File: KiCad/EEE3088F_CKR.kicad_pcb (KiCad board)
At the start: 2 copper layers, 100 x 100 mm, 127 parts, among them J1 Conn_01x02_Pin, J2 Conn_01x02_Pin, J4 Debugger, Q1 AO3401A, Q2 AO3401A, Q3 AO3401A, Q4 AO3401A, Q5 AO3401A, Q6 AO3401A, Q7 AO3401A, SW1 Reset switch, SW2 switch, SW3 switch, SW4 switch, U1 Battery Charger, U2 LMV321, U3 XC6206PxxxMR, U4 GXHTC3, U5 LTR-303ALS-01, U7 24LC256, U8 usb, U9 HT42B534-2, u6 battery holder

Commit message: a few random vias
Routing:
- net GND: vias 6 -> 12
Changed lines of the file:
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@@
     (fp_arc (start 1.080188 -0.709627) (mid 1.299286 -0.618875) (end 1.390018 -0.399772)
       (stroke (width 0.254) (type solid)) (layer "F.SilkS"))
-    (fp_arc (start 1.390018 0.400203) (mid 1.299267 0.61928) (end 1.080188 0.710033)
+    (fp_arc (start 1.390018 0.400203) (mid 1.299267 0.619284) (end 1.080188 0.710033)
       (stroke (width 0.254) (type solid)) (layer "F.SilkS"))
     (fp_circle (center -0.800102 0.400051) (end -0.77013 0.400051)
@@
     (fp_arc (start 1.080188 -0.709627) (mid 1.299286 -0.618875) (end 1.390018 -0.399772)
       (stroke (width 0.254) (type solid)) (layer "F.SilkS"))
-    (fp_arc (start 1.390018 0.400203) (mid 1.299267 0.61928) (end 1.080188 0.710033)
+    (fp_arc (start 1.390018 0.400203) (mid 1.299267 0.619284) (end 1.080188 0.710033)
       (stroke (width 0.254) (type solid)) (layer "F.SilkS"))
     (fp_circle (center -0.800102 0.400051) (end -0.77013 0.400051)
@@
     (fp_arc (start 1.080188 -0.709627) (mid 1.299286 -0.618875) (end 1.390018 -0.399772)
       (stroke (width 0.254) (type solid)) (layer "F.SilkS"))
-    (fp_arc (start 1.390018 0.400203) (mid 1.299267 0.61928) (end 1.080188 0.710033)
+    (fp_arc (start 1.390018 0.400203) (mid 1.299267 0.619284) (end 1.080188 0.710033)
       (stroke (width 0.254) (type solid)) (layer "F.SilkS"))
     (fp_circle (center -0.800102 0.400051) (end -0.77013 0.400051)
@@
     (fp_arc (start 1.080188 -0.709627) (mid 1.299286 -0.618875) (end 1.390018 -0.399772)
       (stroke (width 0.254) (type solid)) (layer "F.SilkS"))
-    (fp_arc (start 1.390018 0.400203) (mid 1.299267 0.619284) (end 1.080188 0.710033)
+    (fp_arc (start 1.390018 0.400203) (mid 1.299267 0.61928) (end 1.080188 0.710033)
       (stroke (width 0.254) (type solid)) (layer "F.SilkS"))
     (fp_circle (center -0.800102 0.400051) (end -0.77013 0.400051)
@@
   )
   (via (at -110.5 116) (size 0.8) (drill 0.4) (layers "F.Cu" "B.Cu") (free) (net 1))
+  (via (at -100.5 95.5) (size 0.8) (drill 0.4) (layers "F.Cu" "B.Cu") (free) (net 1))
+  (via (at -117.5 88.5) (size 0.8) (drill 0.4) (layers "F.Cu" "B.Cu") (free) (net 1))
   (via (at -111 123) (size 0.8) (drill 0.4) (layers "F.Cu" "B.Cu") (free) (net 1))
+  (via (at -118 79.5) (size 0.8) (drill 0.4) (layers "F.Cu" "B.Cu") (free) (net 1))
+  (via (at -105.5 125) (size 0.8) (drill 0.4) (layers "F.Cu" "B.Cu") (free) (net 1))
+  (via (at -97.5 110.5) (size 0.8) (drill 0.4) (layers "F.Cu" "B.Cu") (free) (net 1))
+  (via (at -71.5 113) (size 0.8) (drill 0.4) (layers "F.Cu" "B.Cu") (free) (net 1))
   (via (at -111.5 93) (size 0.8) (drill 0.4) (layers "F.Cu" "B.Cu") (free) (net 1))
   (via (at -110 120.5) (size 0.8) (drill 0.4) (layers "F.Cu" "B.Cu") (free) (net 1))

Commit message: week 5 writeup and a lot of changes to PCB design
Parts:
- moved U2 212.3 mm to (166.2, 83.0)
- moved R10 212.3 mm to (179.5, 74.0)
- moved C4 211.3 mm to (172.8, 99.4)
- moved D2 211.3 mm to (159.4, 82.9)
- moved R13 211.3 mm to (180.1, 65.7)
- moved R16 211.3 mm to (165.8, 62.8)
- moved R19 211.3 mm to (168.1, 66.4)
- moved R48 211.3 mm to (145.2, 78.1)
- moved R49 211.3 mm to (145.1, 75.6)
- moved R55 211.3 mm to (124.7, 123.9)
- moved R56 211.3 mm to (146.3, 93.3)
- moved R57 211.3 mm to (146.3, 90.8)
- moved R6 211.3 mm to (159.4, 78.5)
- moved R63 211.3 mm to (145.1, 95.9)
- moved R64 211.3 mm to (124.0, 118.8)
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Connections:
- U1 pad 9: (no net) -> GND
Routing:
- net /Microcontroller/SDA_2: track 48.8 -> 65.7 mm
- net GND: track 5.60 -> 19.7 mm, vias 12 -> 45
- net /Microcontroller/SCL_1: track 96.3 -> 108.5 mm, vias 3 -> 5
- net Net-(U1-BAT): track 31.9 -> 37.8 mm
- net +3V3: track 391.3 -> 387.8 mm
- net /Sensors/Light_SCL: track 13.8 -> 16.8 mm
- net Net-(U7-SCL): track 12.3 -> 14.9 mm
- net Net-(#FLG06-pwr): track 13.1 -> 15.5 mm
- net Net-(U2-+): track 5.48 -> 7.36 mm
- net /Microcontroller/SDA_1: track 83.9 -> 85.6 mm, vias 3 -> 5
- net Net-(U2--): track 7.32 -> 8.80 mm, vias 0 -> 2
- net Net-(U1-PROG): track 1.69 -> 3.16 mm
- net /Microcontroller/INT_1: track 64.1 -> 65.4 mm, vias 1 -> 3
- net /Microcontroller/Lght_P_1: track 26.1 -> 24.8 mm
- net Net-(U7-SDA): track 9.53 -> 10.6 mm
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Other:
- board text added: "Robert Dugmore DGMROB001 Cameron Clark CLRCAM007 Kian Frassek FRSKIA001 EEE3088F Sensor PCB v0.1"

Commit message: powwer 5v line seperation
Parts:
- moved U2 212.3 mm to (-45.7, 96.5)
- moved R10 212.3 mm to (-32.3, 88.5)
- moved C4 211.3 mm to (-38.1, 112.9)
- moved D2 211.3 mm to (-51.5, 96.4)
- moved R13 211.3 mm to (-30.8, 79.2)
- moved R16 211.3 mm to (-45.0, 76.3)
- moved R19 211.3 mm to (-42.8, 79.9)
- moved R48 211.3 mm to (-65.7, 91.6)
- moved R49 211.3 mm to (-65.8, 89.1)
- moved R55 211.3 mm to (-86.2, 137.4)
- moved R56 211.3 mm to (-64.6, 106.8)
- moved R57 211.3 mm to (-64.6, 104.3)
- moved R6 211.3 mm to (-51.5, 92.0)
- moved R63 211.3 mm to (-65.8, 109.4)
- moved R64 211.3 mm to (-86.9, 132.3)
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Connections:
- U1 pad 9: GND -> (no net)
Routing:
- net /Microcontroller/SDA_2: track 65.7 -> 48.8 mm
- net GND: track 19.7 -> 5.60 mm, vias 45 -> 12
- net /Microcontroller/SCL_1: track 108.5 -> 96.3 mm, vias 5 -> 3
- net Net-(U1-BAT): track 37.8 -> 31.9 mm
- net +3V3: track 387.8 -> 391.3 mm
- net /Sensors/Light_SCL: track 16.8 -> 13.8 mm
- net Net-(U7-SCL): track 14.9 -> 12.3 mm
- net Net-(#FLG06-pwr): track 15.5 -> 13.1 mm
- net Net-(U2-+): track 7.36 -> 5.48 mm
- net /Microcontroller/SDA_1: track 85.6 -> 83.9 mm, vias 5 -> 3
- net Net-(U2--): track 8.80 -> 7.32 mm, vias 2 -> 0
- net Net-(U1-PROG): track 3.16 -> 1.69 mm
- net /Microcontroller/INT_1: track 65.4 -> 64.1 mm, vias 3 -> 1
- net /Microcontroller/Lght_P_1: track 24.8 -> 26.1 mm
- net Net-(U7-SDA): track 10.6 -> 9.53 mm
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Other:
- board text removed: "Robert Dugmore DGMROB001 Cameron Clark CLRCAM007 Kian Frassek FRSKIA001 EEE3088F Sensor PCB v0.1"

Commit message: Final schematic changes and start board design
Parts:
- removed R63: 8.2k, footprint:R0402
- removed R64: 10k, footprint:R0805
- removed R65, R66, R67, R68, R69, R70, R71, R72: 0, footprint:R0603
- removed TP23: STM32 Tx, footprint:Testpoint_2.54mm
- removed TP24: STM32 Rx, footprint:Testpoint_2.54mm
- removed TP25: EEPROM SDA, footprint:Testpoint_2.54mm
- removed TP26: EEPROM SCL, footprint:Testpoint_2.54mm
- removed TP27: USB D-, footprint:Testpoint_2.54mm
- removed TP28: USB D+, footprint:Testpoint_2.54mm
- removed U3: XC6206PxxxMR, footprint:SOT-23-3_L2.9-W1.6-P1.90-LS2.8-BR
- removed u6: battery holder, footprint:BATTERY-SMD_18650-1S-L77.1-W20.7-1
- added J5: STM-link_debugger, Connector_PinHeader_2.54mm:PinHeader_1x03_P2.54mm_Vertical, F.Cu at (152.0, 93.1)
- added J6: 01x10_male_header, Connector_PinHeader_2.54mm:PinHeader_1x10_P2.54mm_Vertical, F.Cu at (101.6, 108.2)
- added JP1: 01x02_male_header_jumper, Connector_PinHeader_2.54mm:PinHeader_1x02_P2.54mm_Vertical, F.Cu at (141.4, 85.9)
- added JP2: 01x02_male_header_jumper, Connector_PinHeader_2.54mm:PinHeader_1x02_P2.54mm_Vertical, F.Cu at (146.0, 85.9)
- added JP3: 01x02_male_header_jumper, Connector_PinHeader_2.54mm:PinHeader_1x02_P2.54mm_Vertical, F.Cu at (150.7, 85.9)
- added JP4: 01x02_male_header_jumper, Connector_PinHeader_2.54mm:PinHeader_1x02_P2.54mm_Vertical, F.Cu at (155.3, 85.9)
- added JP5: 01x03_male_header_jumper, Connector_PinHeader_2.54mm:PinHeader_1x03_P2.54mm_Vertical, F.Cu at (106.2, 108.2)
- added JP6: 01x03_male_header_jumper, Connector_PinHeader_2.54mm:PinHeader_1x03_P2.54mm_Vertical, F.Cu at (110.9, 108.2)
- added Q8: AO3401A, JLCPartFootprints:SOT-23_L2.9-W1.3-P1.90-LS2.4-BR, F.Cu at (128.9, 120.8)
- added R51: 3.9k, JLCPartFootprints:R0402, F.Cu at (149.9, 62.3)
- added R54: 8.2k, JLCPartFootprints:R0402, F.Cu at (149.9, 64.4)
- added R59: 0, JLCPartFootprints:R0603, F.Cu at (148.9, 77.4)
- added R60: 10k, JLCPartFootprints:R0805, F.Cu at (112.9, 131.5)
- added R61: 20k, JLCPartFootprints:R0603, F.Cu at (115.2, 107.1)
- added R62: 0, JLCPartFootprints:R0603, F.Cu at (115.2, 109.6)
- added TP12: LED 2, CustomFootprints:Testpoint, F.Cu at (150.2, 46.3)
- added TP13: Switch 1, CustomFootprints:Testpoint, F.Cu at (150.2, 50.0)
- added U6: LTR-303ALS-01, JLCPartFootprints:SOT-363_L2.0-W1.3-P0.65-LS2.1-BL, F.Cu at (142.7, 122.3)
- added u3: battery holder, JLCPartFootprints:BATTERY-SMD_18650-1S-L77.1-W20.7-1, F.Cu at (74.5, 85.2)
- C1, C2, C3, C4: value 10uf -> 10u; footprint footprint:C0603 -> JLCPartFootprints:C0603
- C5: footprint footprint:C0402_NEW -> JLCPartFootprints:C0402
- C6: footprint footprint:C0402 -> JLCPartFootprints:C0402
- D1: value LED Green -> zener diode; footprint footprint:LED0805-R-RD -> JLCPartFootprints:SOD-123_L2.8-W1.8-LS3.7-RD
- D2: value zener diode -> LED_green; footprint footprint:SOD-123_L2.8-W1.8-LS3.7-RD -> JLCPartFootprints:LED0603-RD
- D3: value LED RED -> LED_red; footprint footprint:LED0603-RD -> JLCPartFootprints:LED0603-RD
- D4, D5: value LED -> LED_white; footprint footprint:LED0603-RD -> JLCPartFootprints:LED0805-R-RD
- J1, J2: value Conn_01x02_Pin -> 01x02_male_header; footprint footprint:HDR-TH_2P-P2.54-V-M -> Connector_PinHeader_2.54mm:PinHeader_1x02_P2.54mm_Vertical
- J3: value ~ -> STM32F051C6_female_header; footprint footprint:STM32F051C6_female_header -> CustomFootprints:STM32F051C6_female_header
- J4: value Debugger -> STM32F051C6_testpoints; footprint footprint:HDR-TH_3P-P2.54_CS-1165SDIG -> CustomFootprints:STM32F051C6_testpoints
- Q1, Q2, Q3, Q4, Q5, Q6, Q7: footprint footprint:SOT-23_L2.9-W1.3-P1.90-LS2.4-BR -> JLCPartFootprints:SOT-23_L2.9-W1.3-P1.90-LS2.4-BR
- R1, R16, R18, R2, R20, R21, R23, R24, R26, R27, R29, R30, R31, R32, R33, R34, R35, R36, R37, R40, R41, R42, R43, R44, R45, R46, R47: footprint footprint:R0603 -> JLCPartFootprints:R0603
- R10, R15, R19, R56, R57: value 1.2k -> 0; footprint footprint:R0805 -> JLCPartFootprints:R0603
- R11, R3: value R1M -> 1.2k; footprint footprint:R0805 -> JLCPartFootprints:R0805
- R12: value R3M -> 1M; footprint footprint:R0603 -> JLCPartFootprints:R0805
- R13: value 0 -> 3M; footprint footprint:R0603 -> JLCPartFootprints:R0603
- R14, R17, R22, R38, R39, R9: value 0 -> 1.2k; footprint footprint:R0603 -> JLCPartFootprints:R0805
- R25: value 100k -> 0; footprint footprint:R1206 -> JLCPartFootprints:R0603
- R28: value 0 -> 100k; footprint footprint:R0603 -> JLCPartFootprints:R1206
- R4: value R2M -> 0; footprint footprint:R0805 -> JLCPartFootprints:R0603
- R48, R55: value 3.9k -> 0; footprint footprint:R0402 -> JLCPartFootprints:R0603
- R49: value 3.9k -> 10k; footprint footprint:R0402 -> JLCPartFootprints:R0805
- R5: value 1.2k -> 1M; footprint footprint:R0805 -> JLCPartFootprints:R0805
- R50, TH1: footprint footprint:R0402 -> JLCPartFootprints:R0402
- R58: value 8.2k -> 0; footprint footprint:R0402 -> JLCPartFootprints:R0603
- R6: value 27.5k -> 2M; footprint footprint:R0805 -> JLCPartFootprints:R0805
- R7: value 10k -> 27.5k; footprint footprint:R0805 -> JLCPartFootprints:R0805
- R8: value 1.2k -> 10k; footprint footprint:R0805 -> JLCPartFootprints:R0805
- RV1: footprint footprint:RES-ADJ-TH_RK09K1130AJ3 -> JLCPartFootprints:RES-ADJ-TH_RK09K1130AJ3
- SW1: footprint footprint:SW-SMD_4P-L5.1-W5.1-P3.70-LS6.5-TL-2 -> JLCPartFootprints:SW-SMD_4P-L5.1-W5.1-P3.70-LS6.5-TL-2
- SW2, SW3, SW4: value switch -> Switch; footprint footprint:SW-SMD_4P-L5.1-W5.1-P3.70-LS6.5-TL-2 -> JLCPartFootprints:SW-SMD_4P-L5.1-W5.1-P3.70-LS6.5-TL-2
- TP1, TP5: footprint footprint:Testpoint_2.54mm -> CustomFootprints:Testpoint
- TP10: value Light SCL -> Light Interrupt; footprint footprint:Testpoint_2.54mm -> CustomFootprints:Testpoint
- TP11: value Light Interrupt -> LED 1; footprint footprint:Testpoint_2.54mm -> CustomFootprints:Testpoint
- TP14: value NSRT -> Switch 2; footprint footprint:Testpoint_2.54mm -> CustomFootprints:Testpoint
- TP15: value Switch1 -> Switch 3; footprint footprint:Testpoint_2.54mm -> CustomFootprints:Testpoint
- TP16: value Switch2 -> uc Tx; footprint footprint:Testpoint_2.54mm -> CustomFootprints:Testpoint
- TP17: value Switch3 -> uc Rx; footprint footprint:Testpoint_2.54mm -> CustomFootprints:Testpoint
- TP18: value STM32 3V3 -> Plug Detect; footprint footprint:Testpoint_2.54mm -> CustomFootprints:Testpoint
- TP19: value STM32 LED1 -> EEPROM SDA; footprint footprint:Testpoint_2.54mm -> CustomFootprints:Testpoint
- TP2: value battery charger -> UVLO; footprint footprint:Testpoint_2.54mm -> CustomFootprints:Testpoint
- TP20: value STM32 LED2 -> EEPROM SCL; footprint footprint:Testpoint_2.54mm -> CustomFootprints:Testpoint
- TP21: value STM32 GND -> USB D-; footprint footprint:Testpoint_2.54mm -> CustomFootprints:Testpoint
- TP22: value STM32 BOOT0 -> USB D+; footprint footprint:Testpoint_2.54mm -> CustomFootprints:Testpoint
- TP3: value UVLO -> battery charger; footprint footprint:Testpoint_2.54mm -> CustomFootprints:Testpoint
- TP4: value +battery out -> 3.3v out; footprint footprint:Testpoint_2.54mm -> CustomFootprints:Testpoint
- TP6: value 3.3v out -> Pot ADC; footprint footprint:Testpoint_2.54mm -> CustomFootprints:Testpoint
- TP7: value Pot ADC -> Sensors SDA; footprint footprint:Testpoint_2.54mm -> CustomFootprints:Testpoint
- TP8: value Therm ADC -> Sensors SCL; footprint footprint:Testpoint_2.54mm -> CustomFootprints:Testpoint
- TP9: value Light SDA -> Therm ADC; footprint footprint:Testpoint_2.54mm -> CustomFootprints:Testpoint
- U1: value Battery Charger -> LMV321IDBVR; footprint footprint:ESOP-8_L4.9-W3.9-P1.27-LS6.0-BL-EP -> JLCPartFootprints:SOT-23-5_L3.0-W1.7-P0.95-LS2.8-BR
- U2: value LMV321 -> Battery Charger; footprint footprint:SOT-23-5_L3.0-W1.7-P0.95-LS2.8-BR -> JLCPartFootprints:ESOP-8_L4.9-W3.9-P1.27-LS6.0-BL-EP
- U4: value GXHTC3 -> XC6206PxxxMR; footprint footprint:DFN-6_L2.0-W2.0-P0.50-BL-EP -> JLCPartFootprints:SOT-23-3_L2.9-W1.6-P1.90-LS2.8-BR
- U5: value LTR-303ALS-01 -> GXHTC3; footprint footprint:SOT-363_L2.0-W1.3-P0.65-LS2.1-BL -> JLCPartFootprints:DFN-6_L2.0-W2.0-P0.50-BL-EP
- U7: footprint footprint:PDIP-8_L9.3-W6.4-P2.54-LS7.6-BL -> JLCPartFootprints:PDIP-8_L9.3-W6.4-P2.54-LS7.6-BL
- U8: footprint footprint:MICRO-USB-SMD_MICROXNJ -> JLCPartFootprints:MICRO-USB-SMD_MICROXNJ
- U9: footprint footprint:SOIC-8_L4.9-W3.9-P1.27-LS6.0-BL -> JLCPartFootprints:SOP-8_L4.9-W3.9-P1.27-LS6.0-BL
- moved TP11 269.5 mm to (150.2, 42.7)
- moved R38 265.6 mm to (153.2, 67.8)
- moved C5 256.9 mm to (138.9, 121.5), turned to 0 degrees
- moved U7 256.0 mm to (144.4, 96.0)
- moved R43 255.3 mm to (144.9, 70.0)
- moved R45 255.2 mm to (144.9, 74.9)
- moved C6 255.0 mm to (138.9, 123.7), turned to 0 degrees
- moved R39 254.4 mm to (153.2, 70.7)
- moved R47 253.4 mm to (144.9, 79.9)
- moved R42 252.6 mm to (144.9, 67.5)
- moved TH1 252.5 mm to (142.2, 125.4), turned to 0 degrees
- moved R36 251.7 mm to (141.0, 74.9)
- moved R46 250.8 mm to (144.9, 77.4)
- moved R33 250.6 mm to (141.0, 67.5)
- moved RV1 249.5 mm to (138.3, 115.5)
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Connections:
- C1 pad 1: Net-(D1-A) -> Net-(D2-A)
- C2 pad 1: Net-(U1-BAT) -> Net-(J1-Pin_2)
- C3 pad 1: Net-(#FLG01-pwr) -> Net-(U4-VI)
- C4 pad 1: +3V3 -> Net-(U4-VO)
- C5 pad 1: Net-(#FLG04-pwr) -> Net-(Q7-D)
- C6 pad 1: Net-(#FLG06-pwr) -> Net-(Q8-D)
- D1 pad 1: Net-(D1-K) -> Net-(U1--)
- D1 pad 2: Net-(D1-A) -> Net-(D1-Pad2)
- D2 pad 1: Net-(U2--) -> Net-(D2-K)
- D2 pad 2: Net-(D2-Pad2) -> Net-(D2-A)
- D3 pad 2: Net-(D1-A) -> Net-(D2-A)
- J3 pad 10: /Microcontroller/THM_2 -> /Microcontroller/uc10
- J3 pad 11: /Microcontroller/POT_2 -> /Microcontroller/uc11
- J3 pad 12: /Microcontroller/Tx_2 -> /Microcontroller/uc12
- J3 pad 13: /Microcontroller/Rx_2 -> /Microcontroller/uc13
- J3 pad 14: /Microcontroller/INT_2 -> /Microcontroller/uc14
- J3 pad 15: /Microcontroller/LED1_1 -> /Microcontroller/LED1
- J3 pad 16: /Microcontroller/LED2_1 -> /Microcontroller/LED2
- J3 pad 17: unconnected-(J3-_PA7-Pad17) -> /Microcontroller/uc17
- J3 pad 18: /Microcontroller/THM_1 -> /Microcontroller/THM_uc
- J3 pad 19: /Microcontroller/POT_1 -> /Microcontroller/POT_uc
- J3 pad 2: unconnected-(J3-_PC13-Pad2) -> /Microcontroller/uc2
- J3 pad 20: /Microcontroller/POT_P_1 -> /Microcontroller/POT_P
- J3 pad 21: /Microcontroller/SCL_1 -> /Microcontroller/Plg_Dtct
- J3 pad 22: /Microcontroller/SDA_1 -> /Microcontroller/uc22
- J3 pad 25: /Microcontroller/INT_1 -> /Microcontroller/INT
- J3 pad 29: /Microcontroller/POT_P_2 -> /Microcontroller/uc29
- J3 pad 3: unconnected-(J3-_PC14-Pad3) -> /Microcontroller/uc3
- J3 pad 30: /Microcontroller/THM_P_2 -> /Microcontroller/uc30
- J3 pad 31: /Microcontroller/Lght_P_2 -> /Microcontroller/uc31
- J3 pad 32: /Microcontroller/TeHu_P_2 -> /Microcontroller/uc32
- J3 pad 33: unconnected-(J3-PA12_-Pad33) -> /Microcontroller/uc33
- J3 pad 35: unconnected-(J3-PA6_-Pad35) -> /Microcontroller/uc35
- J3 pad 36: unconnected-(J3-PF7_-Pad36) -> /Microcontroller/uc36
- J3 pad 38: unconnected-(J3-PA15_-Pad38) -> /Microcontroller/uc38
- J3 pad 39: /Microcontroller/THM_P_1 -> /Microcontroller/THM_P
- J3 pad 4: unconnected-(J3-_PC15-Pad4) -> /Microcontroller/uc4
- J3 pad 40: /Microcontroller/Lght_P_1 -> /Microcontroller/Lght_P
- J3 pad 41: /Microcontroller/TeHu_P_1 -> /Microcontroller/TeHu_P
- J3 pad 42: /Microcontroller/Tx_1 -> /Microcontroller/Tx
- J3 pad 43: /Microcontroller/Rx_1 -> /Microcontroller/Rx
- J3 pad 45: /Microcontroller/SCL_2 -> /Microcontroller/SCL_uc
- J3 pad 46: /Microcontroller/SDA_2 -> /Microcontroller/SDA_uc
- J3 pad 5: unconnected-(J3-_PF0-Pad5) -> /Microcontroller/uc5
- J3 pad 6: unconnected-(J3-_PF1-Pad6) -> /Microcontroller/uc6
- J4 pad 1: /Microcontroller/NSRT -> +3V3
- J4 pad 2: /Microcontroller/SWDIO -> /Microcontroller/uc2
- J4 pad 3: /Microcontroller/SWCLK -> /Microcontroller/uc3
- Q1 pad 2: Net-(#FLG02-pwr) -> Net-(D2-A)
- Q1 pad 3: /Power/3.3V UVLO/polarity protector -> Net-(Q1-D)
- Q2 pad 3: Net-(J1-Pin_2) -> /Power/3.3V UVLO/polarity protector
- Q3 pad 2: Net-(Q3-S) -> /Power/polarity protected battery voltage
- Q3 pad 3: /Power/polarity protected battery voltage -> Net-(Q3-D)
- Q4 pad 1: /Microcontroller/Potentiometer_powerenable -> Net-(Q4-G)
- Q4 pad 2: Net-(Q4-S) -> /Power/polarity protected battery voltage
- Q5 pad 1: /Microcontroller/Thermistor_powerenable -> /Microcontroller/Potentiometer_powerenable
- Q6 pad 1: /Microcontroller/TemperatureHumidity_powerenable -> /Microcontroller/Thermistor_powerenable
- Q6 pad 3: Net-(#FLG04-pwr) -> Net-(Q6-D)
- Q7 pad 1: /Microcontroller/Light_powerenable -> /Microcontroller/TemperatureHumidity_powerenable
- Q7 pad 3: Net-(#FLG06-pwr) -> Net-(Q7-D)
- R1 pad 1: Net-(D1-A) -> Net-(Q1-D)
- R10 pad 1: Net-(U1-PROG) -> /Power/polarity protected battery voltage
- R10 pad 2: GND -> /Power/3.3V UVLO/polarity protector
- R11 pad 1: Net-(Q1-G) -> Net-(U2-CHRG)
- R11 pad 2: Net-(R11-Pad2) -> Net-(D3-K)
- R12 pad 1: Net-(R11-Pad2) -> Net-(Q2-G)
- R12 pad 2: Net-(D2-Pad2) -> Net-(R12-Pad2)
- R13 pad 1: Net-(Q2-S) -> Net-(R12-Pad2)
- R13 pad 2: Net-(U1-BAT) -> Net-(D1-Pad2)
- R14 pad 1: Net-(J1-Pin_2) -> Net-(U2-PROG)
- R14 pad 2: Net-(U1-BAT) -> GND
- R15 pad 1: GND -> Net-(Q3-D)
- R15 pad 2: Net-(Q2-G) -> Net-(J1-Pin_2)
- R16 pad 1: Net-(Q3-S) -> /Power/polarity protected battery voltage
- R17 pad 1: Net-(#FLG01-pwr) -> +5V
- R17 pad 2: /Power/3.3V UVLO/polarity protector -> Net-(Q3-G)
- R18 pad 1: /Power/polarity protected battery voltage -> Net-(U4-VI)
- R18 pad 2: Net-(J1-Pin_2) -> /Power/3.3V UVLO/polarity protector
- R19 pad 1: GND -> Net-(U4-VO)
- R19 pad 2: Net-(Q3-G) -> /Power/3.3V UVLO/polarity protector
- R2 pad 1: Net-(#FLG02-pwr) -> Net-(D2-A)
- R2 pad 2: /Power/polarity protected battery voltage -> +5V
- R20 pad 1: +3V3 -> Net-(Q4-D)
- R20 pad 2: Net-(#FLG01-pwr) -> Net-(D2-A)
- R21 pad 1: Net-(Q4-D) -> /Power/polarity protected battery voltage
- R21 pad 2: +3V3 -> Net-(D2-A)
- R22 pad 1: Net-(Q5-D) -> Net-(Q4-G)
- R22 pad 2: +3V3 -> GND
- R23 pad 1: Net-(Q4-S) -> +3V3
- R23 pad 2: +3V3 -> Net-(U4-VO)
- R24 pad 1: Net-(Q5-S) -> Net-(Q5-D)
- R25 pad 1: /Microcontroller/Thermistor_signal -> Net-(Q6-D)
- R25 pad 2: Net-(Q5-D) -> +3V3
- R26 pad 1: Net-(#FLG04-pwr) -> Net-(Q5-S)
- R27 pad 1: Net-(#FLG06-pwr) -> Net-(Q6-S)
- R28 pad 1: Net-(Q6-S) -> /Microcontroller/Thermistor_signal
- R28 pad 2: +3V3 -> Net-(Q6-D)
- R29 pad 1: Net-(Q7-S) -> Net-(Q7-D)
- R3 pad 1: Net-(#FLG02-pwr) -> Net-(Q1-G)
- R3 pad 2: Net-(U2-+) -> GND
- R30 pad 1: /Sensors/Light_SCL -> Net-(Q8-D)
- R30 pad 2: /Microcontroller/SCL_1 -> +3V3
- R31 pad 1: /Sensors/Light_SDA -> Net-(Q7-S)
- R31 pad 2: /Microcontroller/SDA_1 -> +3V3
- R32 pad 1: /Sensors/Light_interrupt -> Net-(Q8-S)
- R32 pad 2: /Microcontroller/INT_1 -> +3V3
- R33 pad 1: /Sensors/Light_SCL -> /Microcontroller/LED1
- R33 pad 2: /Microcontroller/SCL_2 -> Net-(R33-Pad2)
- R34 pad 1: /Sensors/Light_SDA -> /Microcontroller/LED2
- R34 pad 2: /Microcontroller/SDA_2 -> Net-(R34-Pad2)
- R35 pad 1: /Sensors/Light_interrupt -> Net-(R35-Pad1)
- R35 pad 2: /Microcontroller/INT_2 -> /Microcontroller/SW1
- R36 pad 1: /Microcontroller/Thermistor_signal -> Net-(R36-Pad1)
- R36 pad 2: /Microcontroller/THM_1 -> /Microcontroller/SW2
- R37 pad 1: /Microcontroller/Potentiometer_signal -> Net-(R37-Pad1)
- R37 pad 2: /Microcontroller/POT_1 -> /Microcontroller/SW3
- R38 pad 1: /Microcontroller/Thermistor_signal -> Net-(R33-Pad2)
- R38 pad 2: /Microcontroller/THM_2 -> Net-(D4-A)
- R39 pad 1: /Microcontroller/Potentiometer_signal -> Net-(R34-Pad2)
- R39 pad 2: /Microcontroller/POT_2 -> Net-(D5-A)
- R4 pad 1: Net-(U2-+) -> Net-(Q2-S)
- R4 pad 2: GND -> /Power/polarity protected battery voltage
- R40 pad 1: /Microcontroller/Potentiometer_powerenable -> /Sensors/Light_SCL
- R40 pad 2: /Microcontroller/POT_P_1 -> /Microcontroller/SCL
- R41 pad 1: /Microcontroller/Thermistor_powerenable -> /Sensors/Light_SDA
- R41 pad 2: /Microcontroller/THM_P_1 -> /Microcontroller/SDA
- R42 pad 1: /Microcontroller/Light_powerenable -> /Sensors/Light_interrupt
- R42 pad 2: /Microcontroller/Lght_P_1 -> /Microcontroller/INT
- R43 pad 1: /Microcontroller/TemperatureHumidity_powerenable -> /Microcontroller/Thermistor_signal
- R43 pad 2: /Microcontroller/TeHu_P_1 -> /Microcontroller/THM
- R44 pad 1: /Microcontroller/Potentiometer_powerenable -> /Microcontroller/Potentiometer_signal
- R44 pad 2: /Microcontroller/POT_P_2 -> /Microcontroller/POT
- R45 pad 1: /Microcontroller/Thermistor_powerenable -> /Microcontroller/Potentiometer_powerenable
- R45 pad 2: /Microcontroller/THM_P_2 -> /Microcontroller/POT_P
- R46 pad 1: /Microcontroller/Light_powerenable -> /Microcontroller/Thermistor_powerenable
- R46 pad 2: /Microcontroller/Lght_P_2 -> /Microcontroller/THM_P
- R47 pad 1: /Microcontroller/TemperatureHumidity_powerenable -> /Microcontroller/Light_powerenable
- R47 pad 2: /Microcontroller/TeHu_P_2 -> /Microcontroller/Lght_P
- R48 pad 1: /Microcontroller/SCL_1 -> /Microcontroller/TemperatureHumidity_powerenable
- R48 pad 2: +3V3 -> /Microcontroller/TeHu_P
- R49 pad 1: /Microcontroller/SDA_1 -> GND
- R49 pad 2: +3V3 -> /Microcontroller/BOOT0
- R5 pad 1: Net-(D1-K) -> Net-(Q2-S)
- R5 pad 2: Net-(U1-STDBY#) -> Net-(U1-+)
- R50 pad 1: /Microcontroller/SCL_2 -> /Microcontroller/SCL_uc
- R55 pad 1: /Microcontroller/SDA_2 -> /Microcontroller/Tx
- R55 pad 2: +3V3 -> /Microcontroller/Tx
- R56 pad 1: /Microcontroller/LED1_1 -> /Microcontroller/Rx
- R56 pad 2: Net-(D4-A) -> /Microcontroller/Rx
- R57 pad 1: /Microcontroller/LED2_1 -> /Microcontroller/Plug_Detect
- R57 pad 2: Net-(D5-A) -> /Microcontroller/Plg_Dtct
- R58 pad 1: /Microcontroller/INT_1 -> Net-(U7-SDA)
- R58 pad 2: +3V3 -> /Microcontroller/SDA
- R6 pad 1: Net-(#FLG02-pwr) -> Net-(U1-+)
- R6 pad 2: Net-(U2--) -> GND
- R7 pad 1: Net-(D2-Pad2) -> Net-(Q2-S)
- R7 pad 2: GND -> Net-(U1--)
- R8 pad 1: Net-(U1-CHRG) -> Net-(D1-Pad2)
- R8 pad 2: Net-(D3-K) -> GND
- R9 pad 1: /Power/polarity protected battery voltage -> Net-(D2-K)
- R9 pad 2: /Power/3.3V UVLO/polarity protector -> Net-(U2-STDBY#)
- RV1 pad 1: Net-(Q4-D) -> Net-(Q5-D)
- SW2 pad 2: /Microcontroller/SW1 -> Net-(R35-Pad1)
- SW3 pad 2: /Microcontroller/SW2 -> Net-(R36-Pad1)
- SW4 pad 2: /Microcontroller/SW3 -> Net-(R37-Pad1)
- TP1 pad 1: Net-(D1-A) -> Net-(D2-A)
- TP10 pad 1: /Sensors/Light_SCL -> /Sensors/Light_interrupt
- TP11 pad 1: /Sensors/Light_interrupt -> Net-(R33-Pad2)
- TP14 pad 1: /Microcontroller/NSRT -> /Microcontroller/SW2
- TP15 pad 1: /Microcontroller/SW1 -> /Microcontroller/SW3
- TP16 pad 1: /Microcontroller/SW2 -> /Microcontroller/Tx
- TP17 pad 1: /Microcontroller/SW3 -> /Microcontroller/Rx
- TP18 pad 1: +3V3 -> /Microcontroller/Plug_Detect
- TP19 pad 1: /Microcontroller/LED1_1 -> Net-(U7-SCL)
- TP2 pad 1: Net-(U1-BAT) -> /Power/3.3V UVLO/polarity protector
- TP20 pad 1: /Microcontroller/LED2_1 -> Net-(U7-SDA)
- TP21 pad 1: GND -> Net-(U8-D-)
- TP22 pad 1: /Microcontroller/BOOT0 -> Net-(U8-D+)
- TP3 pad 1: /Power/3.3V UVLO/polarity protector -> Net-(J1-Pin_2)
- TP4 pad 1: Net-(J1-Pin_2) -> Net-(U4-VO)
- TP6 pad 1: +3V3 -> /Microcontroller/Potentiometer_signal
- TP7 pad 1: /Microcontroller/Potentiometer_signal -> /Sensors/Light_SDA
- TP8 pad 1: /Microcontroller/Thermistor_signal -> /Sensors/Light_SCL
- TP9 pad 1: /Sensors/Light_SDA -> /Microcontroller/Thermistor_signal
- U1 pad 1: GND -> Net-(U1-+)
- U1 pad 2: Net-(U1-PROG) -> GND
- U1 pad 3: GND -> Net-(U1--)
- U1 pad 4: Net-(D1-A) -> Net-(R12-Pad2)
- U1 pad 5: Net-(U1-BAT) -> Net-(Q2-S)
- U2 pad 1: Net-(U2-+) -> GND
- U2 pad 2: GND -> Net-(U2-PROG)
- U2 pad 3: Net-(U2--) -> GND
- U2 pad 4: Net-(R11-Pad2) -> Net-(D2-A)
- U2 pad 5: Net-(#FLG02-pwr) -> Net-(J1-Pin_2)
- U4 pad 1: Net-(#FLG04-pwr) -> GND
- U4 pad 2: unconnected-(U4-NC-Pad2) -> Net-(U4-VO)
- U4 pad 3: /Sensors/Light_SCL -> Net-(U4-VI)
- U5 pad 1: Net-(#FLG06-pwr) -> Net-(Q7-D)
- U5 pad 3: GND -> /Sensors/Light_SCL
- U5 pad 4: /Sensors/Light_SCL -> /Sensors/Light_SDA
- U5 pad 5: /Sensors/Light_interrupt -> unconnected-(U5-NC-Pad5)
- U5 pad 6: /Sensors/Light_SDA -> GND
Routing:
- net +3V3: track 391.3 -> 0.00 mm, vias 5 -> 0
- net /Microcontroller/SW2: track 133.4 -> 0.00 mm
- net /Microcontroller/NSRT: track 127.7 -> 0.00 mm, vias 2 -> 0
- net /Microcontroller/SW3: track 123.9 -> 0.00 mm
- net /Microcontroller/THM_2: track 118.9 -> 0.00 mm
- net /Microcontroller/INT_2: track 102.0 -> 0.00 mm, vias 1 -> 0
- net /Microcontroller/THM_1: track 100.9 -> 0.00 mm, vias 1 -> 0
- net /Microcontroller/SCL_1: track 96.3 -> 0.00 mm, vias 3 -> 0
- net /Microcontroller/SW1: track 95.0 -> 0.00 mm
- net /Microcontroller/SDA_1: track 83.9 -> 0.00 mm, vias 3 -> 0
- net /Microcontroller/POT_2: track 80.9 -> 0.00 mm
- net /Microcontroller/Tx_1: track 72.0 -> 0.00 mm, vias 1 -> 0
- net /Microcontroller/Rx_1: track 67.6 -> 0.00 mm, vias 1 -> 0
- net /Microcontroller/INT_1: track 64.1 -> 0.00 mm, vias 1 -> 0
- net /Microcontroller/POT_P_1: track 62.1 -> 0.00 mm, vias 1 -> 0
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- removed copper zone on B.Cu, net GND
- removed copper zone on F.Cu, net GND
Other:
- board outline removed
- board text removed: "3V3 reg."
- board text removed: "Batt RPP"
- board text removed: "Battery Charger"
- board text removed: "Charging RPP"
- board text removed: "UVLO"

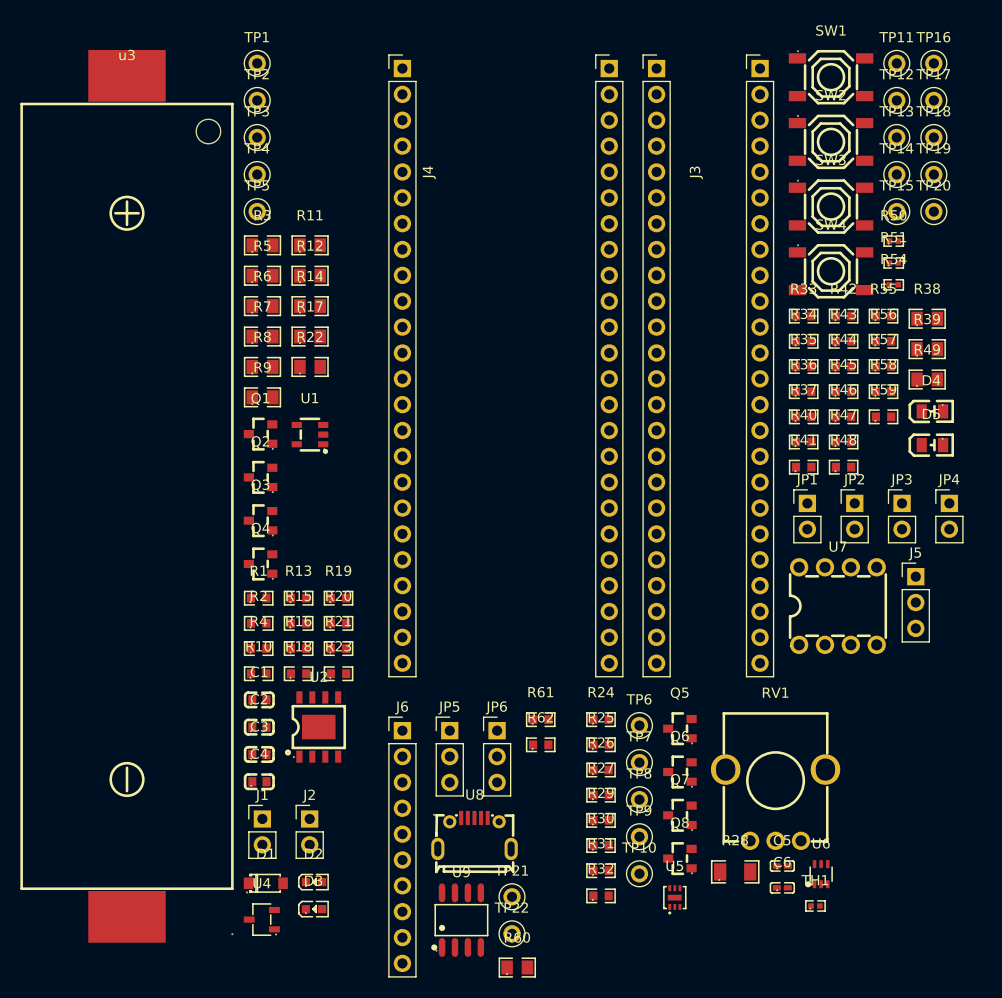
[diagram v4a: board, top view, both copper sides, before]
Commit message: literally just added one 0ohm resistor
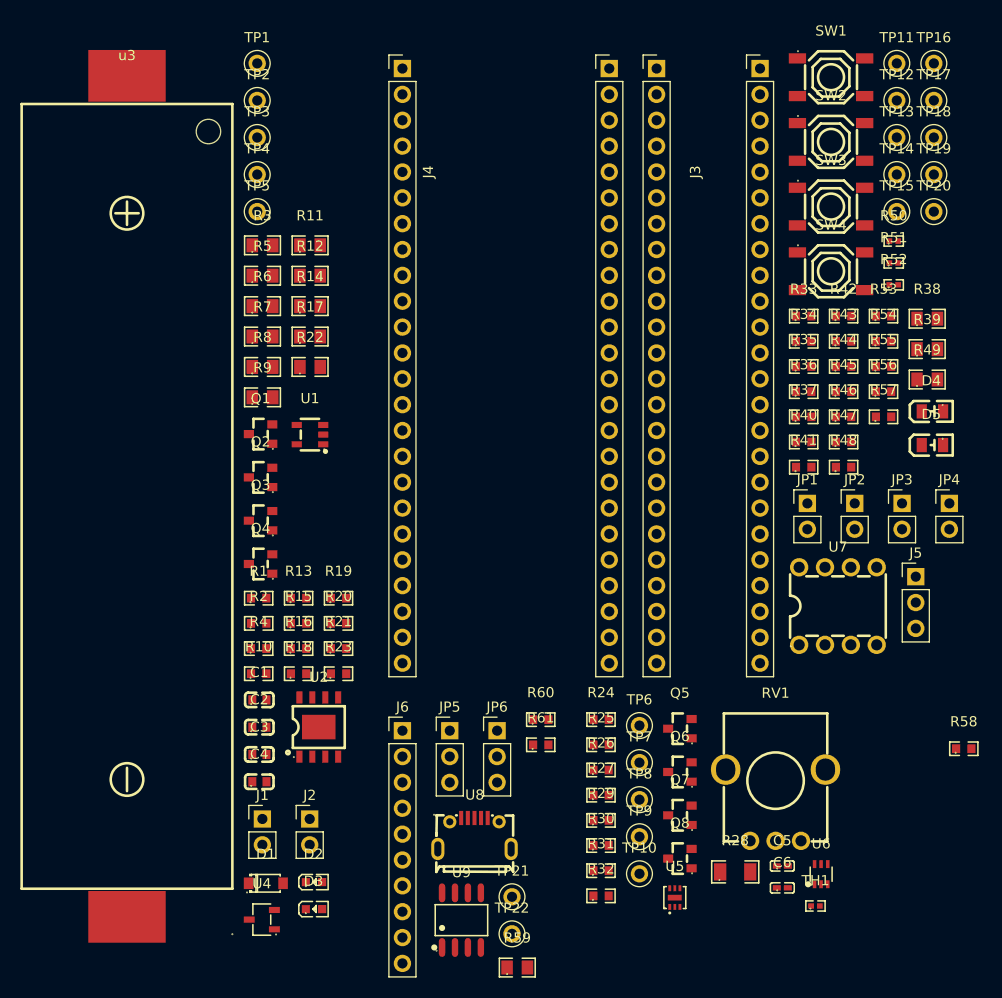
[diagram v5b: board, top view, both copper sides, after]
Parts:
- added R58: 0, JLCPartFootprints:R0603, F.Cu at (156.7, 110.0)
- renumbered R54 to R52, R55 to R53, R56 to R54, R57 to R55, R58 to R56, R59 to R57, R60 to R59, R61 to R60, R62 to R61
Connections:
- J6 pad 7: /Microcontroller/Plug_Detect -> Net-(J6-Pin_7)

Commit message: Lots of PCB design
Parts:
- added C7: 33pF, JLCPartFootprints:C0402, F.Cu at (148.5, 82.0)
- added C8: 33pF, JLCPartFootprints:C0402, F.Cu at (131.5, 82.0)
- added Y1: Crystal, JLCPartFootprints:CRYSTAL-SMD_L11.5-W4.8-LS12.7, F.Cu at (140.0, 82.0)
- moved TP10 133.5 mm to (258.2, 129.5)
- moved Q8 133.5 mm to (262.2, 128.0)
- moved R30 133.5 mm to (254.4, 126.7)
- moved R32 133.5 mm to (254.4, 131.7)
- moved R40 131.6 mm to (245.0, 160.5)
- moved R41 131.6 mm to (245.0, 163.0)
- moved R47 129.1 mm to (268.0, 119.0)
- moved C6 126.9 mm to (265.5, 133.0)
- moved U6 126.9 mm to (269.3, 131.7)
- moved R42 120.9 mm to (249.0, 129.0)
- moved D3 113.7 mm to (149.3, 27.0)
- moved JP3 113.2 mm to (245.0, 148.5)
- moved TP13 112.2 mm to (154.8, 162.1)
- moved TP15 112.2 mm to (154.8, 169.3)
- moved SW2 112.2 mm to (148.3, 162.5)
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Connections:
- net /Microcontroller/uc5 renamed /Microcontroller/OSC_IN
- net /Microcontroller/uc6 renamed /Microcontroller/OSC_OUT
- C1 pad 1: Net-(D2-A) -> /Power/Plug_Detect_5V
- D2 pad 2: Net-(D2-A) -> /Power/Plug_Detect_5V
- D3 pad 2: Net-(D2-A) -> /Power/Plug_Detect_5V
- Q1 pad 2: Net-(D2-A) -> /Power/Plug_Detect_5V
- R2 pad 1: Net-(D2-A) -> /Power/Plug_Detect_5V
- R20 pad 2: Net-(D2-A) -> /Power/Plug_Detect_5V
- R21 pad 2: Net-(D2-A) -> /Power/Plug_Detect_5V
- R59 pad 1: +5V -> /Power/Plug_Detect_5V
- TP1 pad 1: Net-(D2-A) -> /Power/Plug_Detect_5V
- U2 pad 4: Net-(D2-A) -> /Power/Plug_Detect_5V
- U2 pad 8: Net-(D2-A) -> /Power/Plug_Detect_5V
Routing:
- net /Microcontroller/Rx: track 0.00 -> 101.0 mm, vias 0 -> 4
- net +5V: track 0.00 -> 100.5 mm, vias 0 -> 2
- net /Microcontroller/Tx: track 0.00 -> 84.2 mm, vias 0 -> 2
- net Net-(J1-Pin_2): track 0.00 -> 82.7 mm, vias 0 -> 1
- net +3V3: track 0.00 -> 72.1 mm, vias 0 -> 1
- net Net-(U8-D-): track 0.00 -> 56.9 mm, vias 0 -> 2
- net /Power/Plug_Detect_5V: track 0.00 -> 54.0 mm
- net /Power/polarity protected battery voltage: track 0.00 -> 48.2 mm, vias 0 -> 2
- net Net-(U8-D+): track 0.00 -> 46.0 mm, vias 0 -> 2
- net /Microcontroller/SWCLK: track 0.00 -> 39.0 mm, vias 0 -> 2
- net /Microcontroller/SWDIO: track 0.00 -> 37.6 mm, vias 0 -> 2
- net /Microcontroller/NSRT: track 0.00 -> 36.2 mm, vias 0 -> 2
- net Net-(D1-Pad2): track 0.00 -> 23.3 mm
- net Net-(U1-+): track 0.00 -> 20.4 mm, vias 0 -> 2
- net /Microcontroller/Plug_Detect: track 0.00 -> 18.2 mm
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- added copper zone on B.Cu, net GND
- added copper zone on F.Cu, net GND
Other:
- board outline added: 90 x 81 mm

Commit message: finally finished PCB design
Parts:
- moved RV1 131.9 mm to (120.5, 70.0), turned to 90 degrees
- moved R44 131.4 mm to (110.0, 66.2), turned to -90 degrees
- moved TP6 131.2 mm to (107.5, 63.5)
- moved D5 122.6 mm to (192.5, 43.1), turned to 90 degrees
- moved JP2 118.8 mm to (107.5, 70.5)
- moved D4 118.5 mm to (190.0, 43.1), turned to 90 degrees
- moved Q5 116.7 mm to (123.0, 78.0), turned to -90 degrees
- moved R45 109.8 mm to (123.0, 86.5)
- moved R26 108.9 mm to (123.0, 83.0), turned to 180 degrees
- moved R24 108.4 mm to (123.0, 81.0), turned to 180 degrees
- moved U6 108.0 mm to (167.0, 97.0), turned to 90 degrees
- moved R34 107.2 mm to (187.2, 63.5)
- moved R41 106.6 mm to (181.3, 77.5), turned to 180 degrees
- moved TP11 104.7 mm to (192.5, 63.5)
- moved R40 103.1 mm to (181.3, 79.5), turned to 180 degrees
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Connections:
- J3 pad 15: /Microcontroller/LED1 -> /Microcontroller/uc15
- J3 pad 16: /Microcontroller/LED2 -> /Microcontroller/uc16
- J3 pad 20: /Microcontroller/POT_P -> /Microcontroller/TeHu_P
- J3 pad 21: /Microcontroller/Plg_Dtct -> /Microcontroller/INT
- J3 pad 22: /Microcontroller/uc22 -> /Microcontroller/Lght_P
- J3 pad 25: /Microcontroller/INT -> /Microcontroller/LED2
- J3 pad 26: /Microcontroller/SW1 -> /Microcontroller/LED1
- J3 pad 27: /Microcontroller/SW2 -> /Microcontroller/Plg_Dtct
- J3 pad 38: /Microcontroller/uc38 -> /Microcontroller/SW2
- J3 pad 39: /Microcontroller/THM_P -> /Microcontroller/SW1
- J3 pad 40: /Microcontroller/Lght_P -> /Microcontroller/THM_P
- J3 pad 41: /Microcontroller/TeHu_P -> /Microcontroller/POT_P
- J3 pad 42: /Microcontroller/Tx -> /Microcontroller/Tx_uc
- J3 pad 43: /Microcontroller/Rx -> /Microcontroller/Rx_uc
- J4 pad 15: /Microcontroller/LED1 -> /Microcontroller/uc15
- J4 pad 16: /Microcontroller/LED2 -> /Microcontroller/uc16
- J4 pad 20: /Microcontroller/POT_P -> /Microcontroller/TeHu_P
- J4 pad 21: /Microcontroller/Plg_Dtct -> /Microcontroller/INT
- J4 pad 22: /Microcontroller/uc22 -> /Microcontroller/Lght_P
- J4 pad 25: /Microcontroller/INT -> /Microcontroller/LED2
- J4 pad 26: /Microcontroller/SW1 -> /Microcontroller/LED1
- J4 pad 27: /Microcontroller/SW2 -> /Microcontroller/Plg_Dtct
- J4 pad 38: /Microcontroller/uc38 -> /Microcontroller/SW2
- J4 pad 39: /Microcontroller/THM_P -> /Microcontroller/SW1
- J4 pad 40: /Microcontroller/Lght_P -> /Microcontroller/THM_P
- J4 pad 41: /Microcontroller/TeHu_P -> /Microcontroller/POT_P
- J4 pad 42: /Microcontroller/Tx -> /Microcontroller/Tx_uc
- J4 pad 43: /Microcontroller/Rx -> /Microcontroller/Rx_uc
- R53 pad 1: /Microcontroller/Tx -> /Microcontroller/Tx_uc
- R54 pad 1: /Microcontroller/Rx -> /Microcontroller/Rx_uc
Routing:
- net /Microcontroller/THM_uc: track 5.08 -> 191.9 mm, vias 0 -> 5
- net +3V3: track 72.1 -> 256.6 mm, vias 1 -> 3
- net /Microcontroller/POT_uc: track 5.08 -> 188.1 mm, vias 0 -> 5
- net /Microcontroller/SDA_uc: track 5.08 -> 153.6 mm, vias 0 -> 1
- net /Microcontroller/SCL_uc: track 5.08 -> 150.5 mm, vias 0 -> 1
- net /Microcontroller/NSRT: track 36.2 -> 159.3 mm, vias 2 -> 7
- net /Microcontroller/SW3: track 5.08 -> 88.4 mm, vias 0 -> 2
- net /Microcontroller/THM_P: track 5.08 -> 68.7 mm, vias 0 -> 3
- net /Sensors/Light_SDA: track 0.00 -> 63.2 mm, vias 0 -> 2
- net /Sensors/Light_SCL: track 0.00 -> 59.1 mm, vias 0 -> 2
- net /Microcontroller/SW2: track 5.08 -> 62.2 mm, vias 0 -> 2
- net /Microcontroller/SW1: track 5.08 -> 57.1 mm, vias 0 -> 1
- net /Microcontroller/SWDIO: track 37.6 -> 86.5 mm
- net /Microcontroller/Tx: track 84.2 -> 126.8 mm, vias 2 -> 3
- net /Microcontroller/SWCLK: track 39.0 -> 81.4 mm
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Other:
- board size 90 x 81 mm -> 90 x 75 mm
- board text added: "Robert Dugmore - DGMROB001 Cameron Clark - CLRCAM007 Kian Frassek - FRSKIA001 EEE3088F 2023 Group 12 Sensor HAT PCB rev 0.2"
